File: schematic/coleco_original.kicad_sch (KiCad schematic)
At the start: 0 parts

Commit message: first day of pcb trace, working pin by of the z80 cpu. Last pin completed: 7
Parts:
- added J1: Cartridge Port, symbol Connector_Generic:Conn_02x15_Odd_Even
- added J2: Expansion Port, symbol Connector_Generic:Conn_02x30_Counter_Clockwise
- added JP1, JP2: SolderJumper_2_Open, symbol Jumper:SolderJumper_2_Open
- added R26: 470R, symbol Device:R
- added R60: 47R, symbol Device:R
- added U1: Z80CPU, symbol CPU:Z80CPU
- added U18, U19: 74LS541, symbol 74xx:74LS541
- added U2: 27C256, Package_DIP:DIP-28_W15.24mm, symbol Memory_EPROM:27C256
- added U20: SN76489AN, symbol Vintage_PC_Audio:SN76489AN
- added U3, U4: SCM2114AL, symbol Vintage_PC_RAM:SCM2114AL
- added U5: 74LS138, symbol 74xx:74LS138
- added U9: TMS9928A, symbol VINTAGE_PC_VIDEO:TMS9928A
- added WJ4, WJ5: Jumper_2_Bridged_32K_ROM, symbol Jumper:Jumper_2_Bridged
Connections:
- new net: U2.22 (~{OE}), U5.15 (O0), WJ4.2 (B)
- new net: J2.45 (Pin_45), R26.2, R60.2, U1.6 (~{CLK})
- new net: J2.40 (Pin_40), R26.1
- new net: JP1.1 (A), U2.20 (~{CE}), WJ4.1 (A)
- new net: JP2.2 (B), U2.23 (A11), WJ5.2 (B)
- new net +5VD: U2.1 (VPP), U2.26 (A13), U2.27 (A14), U2.28 (VCC)
- new net A0: U1.30 (A0)
- new net A1: U1.31 (A1)
- new net A10: U1.40 (A10)
- new net A11: J1.14 (Pin_14), J2.37 (Pin_37), JP1.2 (B), U1.1 (A11), WJ5.1 (A)
- new net A12: J1.24 (Pin_24), J2.38 (Pin_38), JP2.1 (A), U1.2 (A12), U2.2 (A12)
- new net A13: J1.19 (Pin_19), J2.22 (Pin_22), U1.3 (A13), U5.1 (A0)
- new net A14: J1.20 (Pin_20), J2.4 (Pin_4), U1.4 (A14), U5.2 (A1)
- new net A15: J2.43 (Pin_43), U1.5 (A15), U5.3 (A2)
- new net A2: U1.32 (A2)
- new net A3: U1.33 (A3)
- new net A4: U1.34 (A4)
- new net A5: U1.35 (A5)
- new net A6: U1.36 (A6)
- new net A7: U1.37 (A7)
- new net A8: U1.38 (A8)
- new net A9: U1.39 (A9)
- new net D0: U1.14 (D0), U2.11 (D0), U20.10 (D7), U9.17 (CD7)
- new net D1: U1.15 (D1), U2.12 (D1), U20.11 (D6), U9.18 (CD6)
- new net D2: U1.12 (D2), U2.13 (D2), U20.12 (D5), U9.19 (CD5)
- new net D3: U1.8 (D3), U2.15 (D3), U20.13 (D4), U9.20 (CD4)
- new net D4: J1.6 (Pin_6), J2.19 (Pin_19), U1.7 (D4), U18.15 (Y3), U19.14 (Y4), U2.16 (D4), U20.15 (D3), U4.14 (D0), U9.21 (CD3)
- new net D5: U1.9 (D5), U2.17 (D5), U20.1 (D2), U9.22 (CD2)
- new net D6: U1.10 (D6), U2.18 (D6), U20.2 (D1), U9.23 (CD1)
- new net D7: U1.13 (D7), U2.19 (D7), U20.3 (D0), U9.24 (CD0)

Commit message: revised schematic into sheets for easier design. Looks much better.
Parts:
- removed J1: Cartridge Port, symbol Connector_Generic:Conn_02x15_Odd_Even
- removed J2: Expansion Port, symbol Connector_Generic:Conn_02x30_Counter_Clockwise
- removed JP1, JP2: SolderJumper_2_Open, symbol Jumper:SolderJumper_2_Open
- removed R26: 470R, symbol Device:R
- removed R60: 47R, symbol Device:R
- removed U1: Z80CPU, symbol CPU:Z80CPU
- removed U18, U19: 74LS541, symbol 74xx:74LS541
- removed U2: 27C256, Package_DIP:DIP-28_W15.24mm, symbol Memory_EPROM:27C256
- removed U20: SN76489AN, symbol Vintage_PC_Audio:SN76489AN
- removed U3, U4: SCM2114AL, symbol Vintage_PC_RAM:SCM2114AL
- removed U5: 74LS138, symbol 74xx:74LS138
- removed U9: TMS9928A, symbol VINTAGE_PC_VIDEO:TMS9928A
- removed WJ4, WJ5: Jumper_2_Bridged_32K_ROM, symbol Jumper:Jumper_2_Bridged
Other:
- removed sheet io
- added sheet controller (controller.kicad_sch)
- added sheet decoder_logic (decoder_logic.kicad_sch)
- added sheet io_ports (io_ports.kicad_sch)
- sheet clock_reset ports: added ~{CLK}; removed none
- sheet cpu ports: added A[0..15], D[0..7], ~{CLK}; removed none
- sheet sound ports: added D[0..7]; removed audio, audio_data_bus, clk_audio, nWRITE_audio, ready
- sheet storage ports: added A[0..15], D[0..7], U5_O0; removed none
- sheet video ports: added D[0..7]; removed Y, Yb, Yr, mode, nCSR, nCSW, nINT, video_data_bus

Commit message: Up to pin 29 on z80 done. Address 0 to 10 left. Only tracing to its end point for the most part. Each chip gets traced chip to chip in this manned
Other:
- sheet clock_reset ports: added ~{INT}, ~{M1}, ~{RESET}, ~{RFSH}, ~{WAIT}; removed none
- sheet cpu ports: added ~{BUSAK}, ~{BUSRQ}, ~{HALT}, ~{INT}, ~{IORQ}, ~{M1}, ~{MREQ}, ~{NMI}, ~{RD}, ~{RESET}, ~{RFSH}, ~{WAIT}, ~{WR}; removed none
- sheet decoder_logic ports: added ~{IORQ}, ~{MREQ}, ~{WR}; removed none
- sheet io_ports ports: added WAIT, ~{BUSAK}, ~{BUSRQ}, ~{HALT}, ~{INT}, ~{IORQ}, ~{M1}, ~{MREQ}, ~{NMI}, ~{RD}, ~{RESET}, ~{RFSH}, ~{WR}; removed none
- sheet sound ports: added ~{WAIT}; removed none
- sheet storage ports: added ~{WR}; removed none
- sheet video ports: added ~{NMI}; removed none

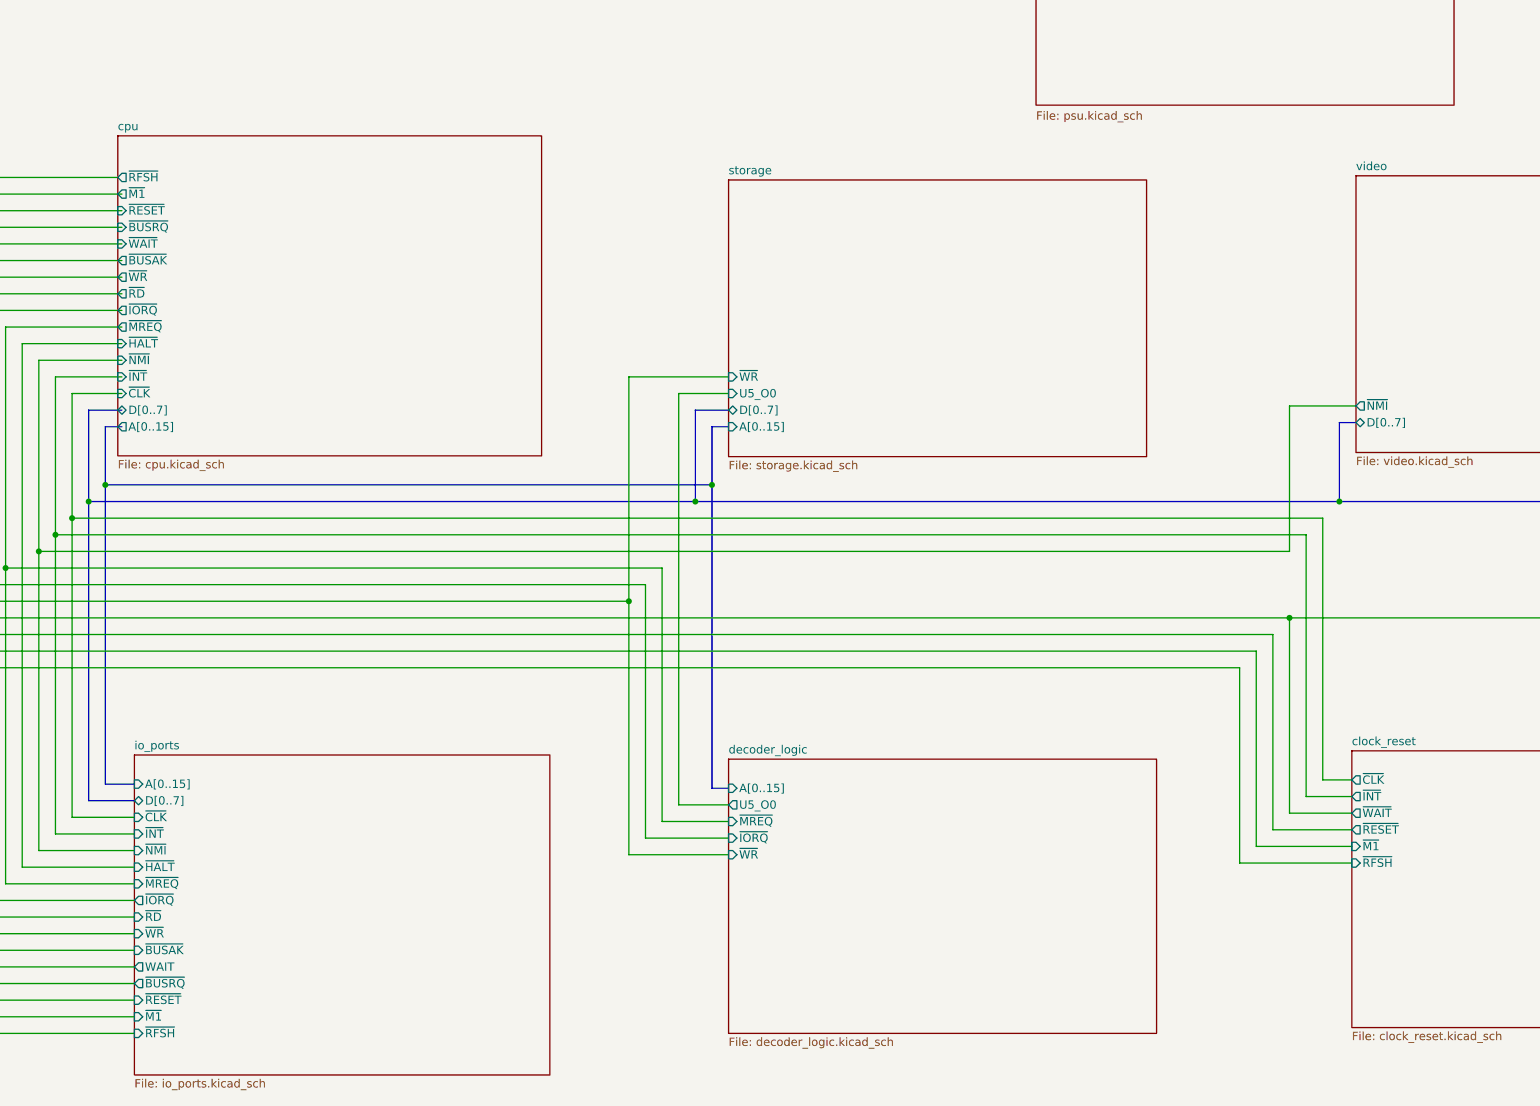
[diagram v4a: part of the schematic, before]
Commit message: completed Z80 trace of PCB. off to a good start.
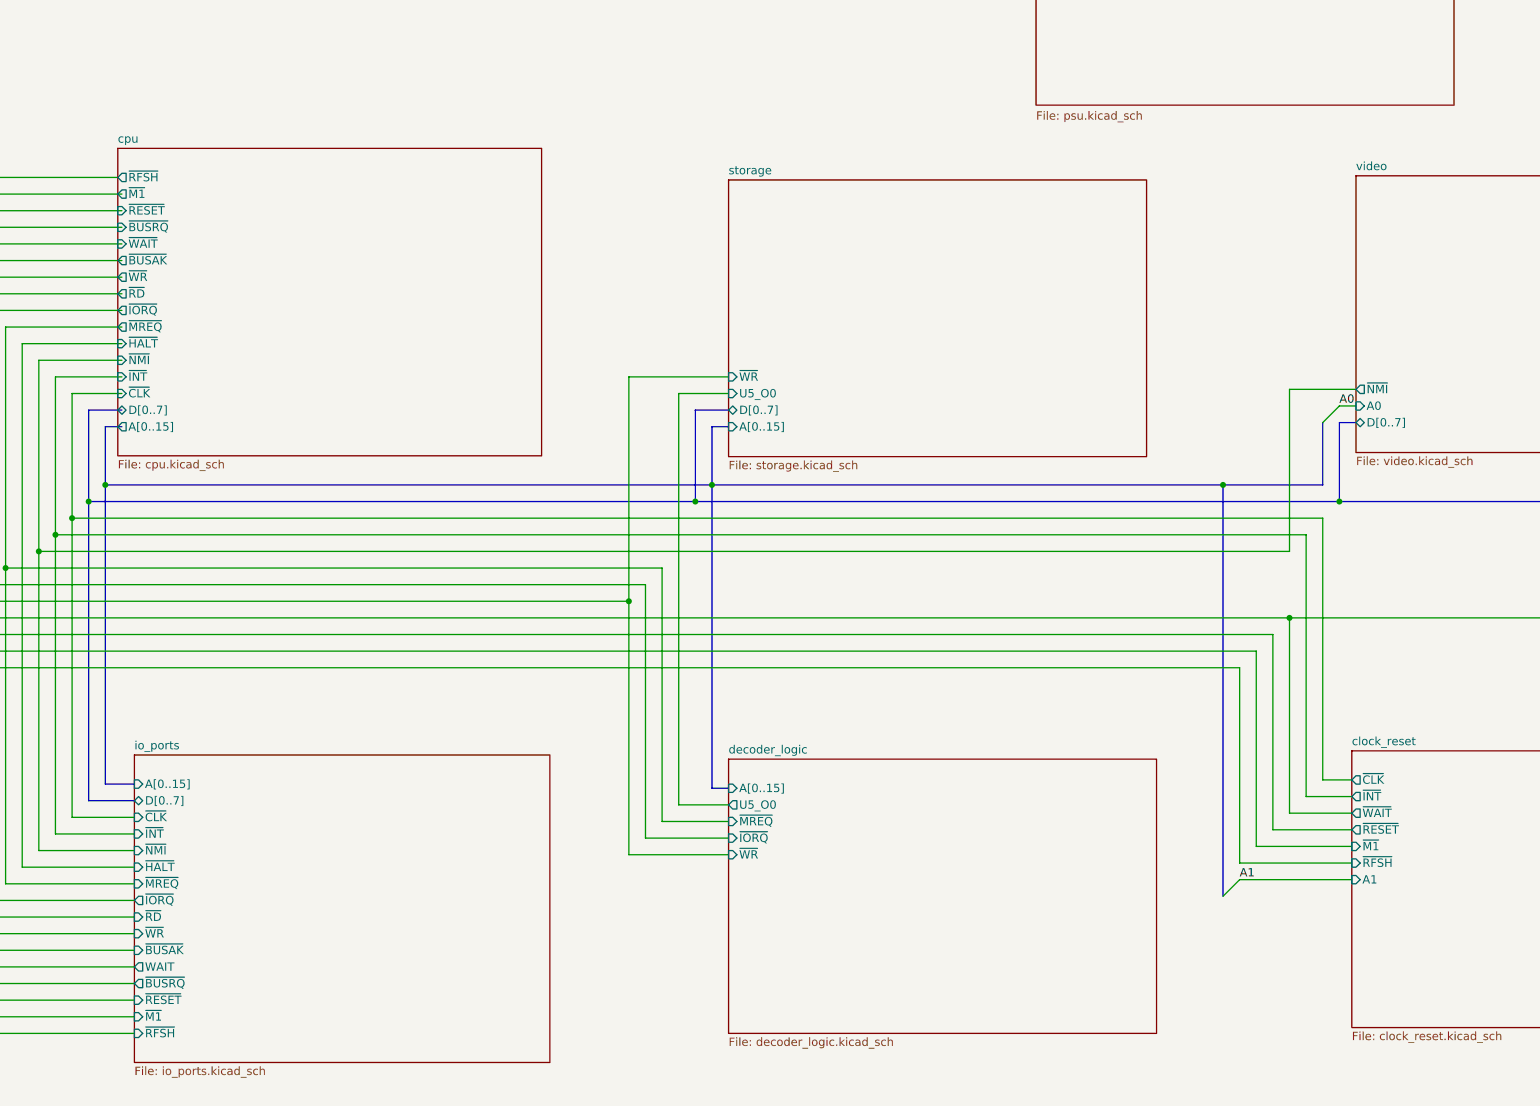
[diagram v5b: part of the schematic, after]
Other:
- sheet clock_reset ports: added A1; removed none
- sheet video ports: added A0; removed none
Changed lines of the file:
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@@
 (kicad_sch (version 20211123) (generator eeschema)
   (paper "B")
+  (junction (at 226.06 123.825) (diameter 0) (color 0 0 0 0)
+  )
   (junction (at 135.255 141.605) (diameter 0) (color 0 0 0 0)
   )
@@
   (junction (at 147.955 123.825) (diameter 0) (color 0 0 0 0)
   )
+  (bus_entry (at 226.06 186.69) (size 2.54 -2.54)
+    (stroke (width 0) (type default) (color 0 0 0 0))
+  )
+  (bus_entry (at 241.3 114.3) (size 2.54 -2.54)
+    (stroke (width 0) (type default) (color 0 0 0 0))
+  )
   (wire (pts (xy 24.765 84.455) (xy 57.785 84.455))
     (stroke (width 0) (type default) (color 0 0 0 0))
@@
     (stroke (width 0) (type default) (color 0 0 0 0))
   )
+  (bus (pts (xy 241.3 114.3) (xy 241.3 123.825))
+    (stroke (width 0) (type default) (color 0 0 0 0))
+  )
   (bus (pts (xy 145.415 112.395) (xy 145.415 126.365))
     (stroke (width 0) (type default) (color 0 0 0 0))
@@
     (stroke (width 0) (type default) (color 0 0 0 0))
   )
+  (bus (pts (xy 226.06 123.825) (xy 241.3 123.825))
+    (stroke (width 0) (type default) (color 0 0 0 0))
+  )
+  (bus (pts (xy 226.06 123.825) (xy 226.06 186.69))
+    (stroke (width 0) (type default) (color 0 0 0 0))
+  )
   (wire (pts (xy 17.145 151.765) (xy 228.6 151.765))
     (stroke (width 0) (type default) (color 0 0 0 0))
@@
     (stroke (width 0) (type default) (color 0 0 0 0))
   )
-  (wire (pts (xy 236.22 133.985) (xy 236.22 111.76))
+  (wire (pts (xy 236.22 133.985) (xy 236.22 109.22))
     (stroke (width 0) (type default) (color 0 0 0 0))
   )
@@
     (stroke (width 0) (type default) (color 0 0 0 0))
   )
+  (bus (pts (xy 147.955 123.825) (xy 226.06 123.825))
+    (stroke (width 0) (type default) (color 0 0 0 0))
+  )
   (bus (pts (xy 243.84 126.365) (xy 243.84 114.3))
     (stroke (width 0) (type default) (color 0 0 0 0))
@@
     (stroke (width 0) (type default) (color 0 0 0 0))
   )
+  (wire (pts (xy 228.6 184.15) (xy 245.745 184.15))
+    (stroke (width 0) (type default) (color 0 0 0 0))
+  )
   (wire (pts (xy 140.335 136.525) (xy 140.335 175.26))
     (stroke (width 0) (type default) (color 0 0 0 0))
@@
     (stroke (width 0) (type default) (color 0 0 0 0))
   )
+  (wire (pts (xy 243.84 111.76) (xy 246.38 111.76))
+    (stroke (width 0) (type default) (color 0 0 0 0))
+  )
   (wire (pts (xy 238.76 131.445) (xy 238.76 171.45))
     (stroke (width 0) (type default) (color 0 0 0 0))
@@
     (stroke (width 0) (type default) (color 0 0 0 0))
   )
-  (wire (pts (xy 236.22 111.76) (xy 246.38 111.76))
+  (wire (pts (xy 236.22 109.22) (xy 246.38 109.22))
     (stroke (width 0) (type default) (color 0 0 0 0))
   )
@@
     (stroke (width 0) (type default) (color 0 0 0 0))
   )
-  (sheet (at 57.15 70.485) (size 64.77 48.895) (fields_autoplaced)
+  (label "A0" (at 243.84 111.76 0)
+    (effects (font (size 1.27 1.27)) (justify left bottom))
+  )
+  (label "A1" (at 228.6 184.15 0)
+    (effects (font (size 1.27 1.27)) (justify left bottom))
+  )
+  (sheet (at 57.15 72.39) (size 64.77 46.99) (fields_autoplaced)
     (stroke (width 0) (type solid) (color 0 0 0 0))
     (fill (color 0 0 0 0.0000))
-    (property "Sheet name" "cpu" (id 0) (at 57.15 69.7734 0)
+    (property "Sheet name" "cpu" (id 0) (at 57.15 71.6784 0)
       (effects (font (size 1.27 1.27)) (justify left bottom))
     )
@@
       (effects (font (size 1.27 1.27)) (justify left))
     )
-    (pin "~{NMI}" output (at 246.38 111.76 180)
+    (pin "~{NMI}" output (at 246.38 109.22 180)
+      (effects (font (size 1.27 1.27)) (justify left))
+    )
+    (pin "A0" input (at 246.38 111.76 180)
       (effects (font (size 1.27 1.27)) (justify left))
     )
@@
       (effects (font (size 1.27 1.27)) (justify left))
     )
+    (pin "A1" input (at 245.745 184.15 180)
+      (effects (font (size 1.27 1.27)) (justify left))
+    )
   )
   (sheet (at 344.17 164.465) (size 64.77 41.91) (fields_autoplaced)
@@
     )
   )
-  (sheet (at 59.69 165.1) (size 63.5 48.895) (fields_autoplaced)
+  (sheet (at 59.69 165.1) (size 63.5 46.99) (fields_autoplaced)
     (stroke (width 0.1524) (type solid) (color 0 0 0 0))
     (fill (color 0 0 0 0.0000))
@@
       (effects (font (size 1.27 1.27)) (justify left bottom))
     )
-    (property "Sheet file" "io_ports.kicad_sch" (id 1) (at 59.69 214.5796 0)
-      (effects (font (size 1.27 1.27)) (justify left top))
-    )
+    (property "Sheet file" "io_ports.kicad_sch" (id 1) (at 59.69 212.6746 0)
+      (effects (font (size 1.27 1.27)) (justify left top))
+    )

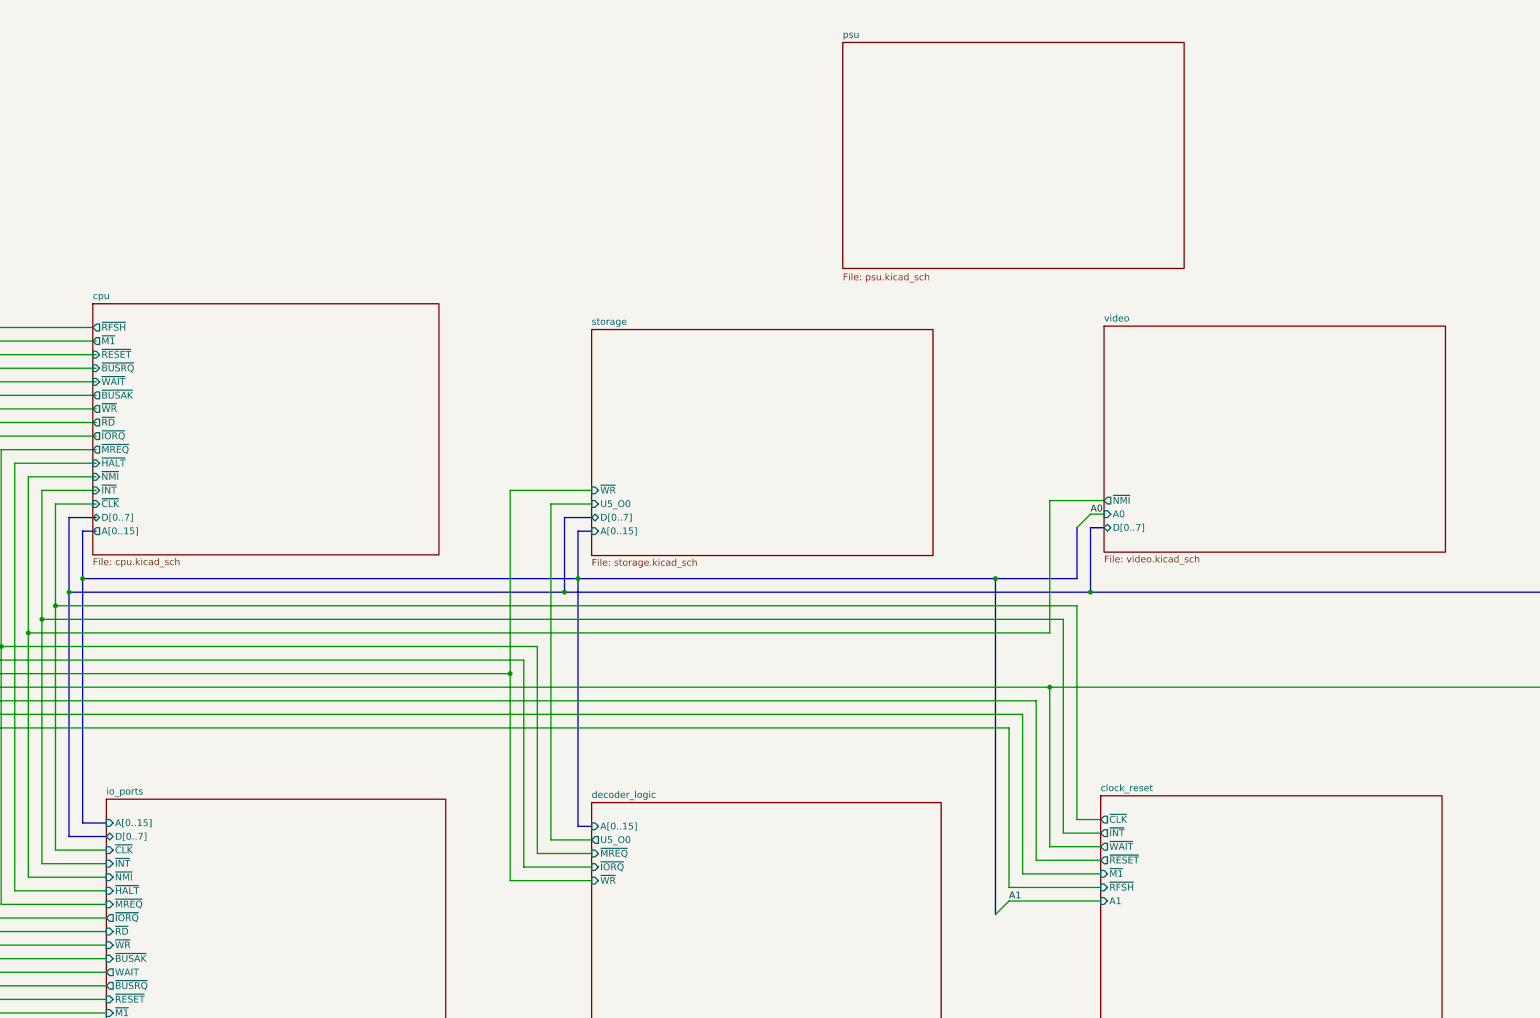
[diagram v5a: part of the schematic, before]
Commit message: added rf modulation schematic, added dram to vdp. Fixed +5vc to +5v
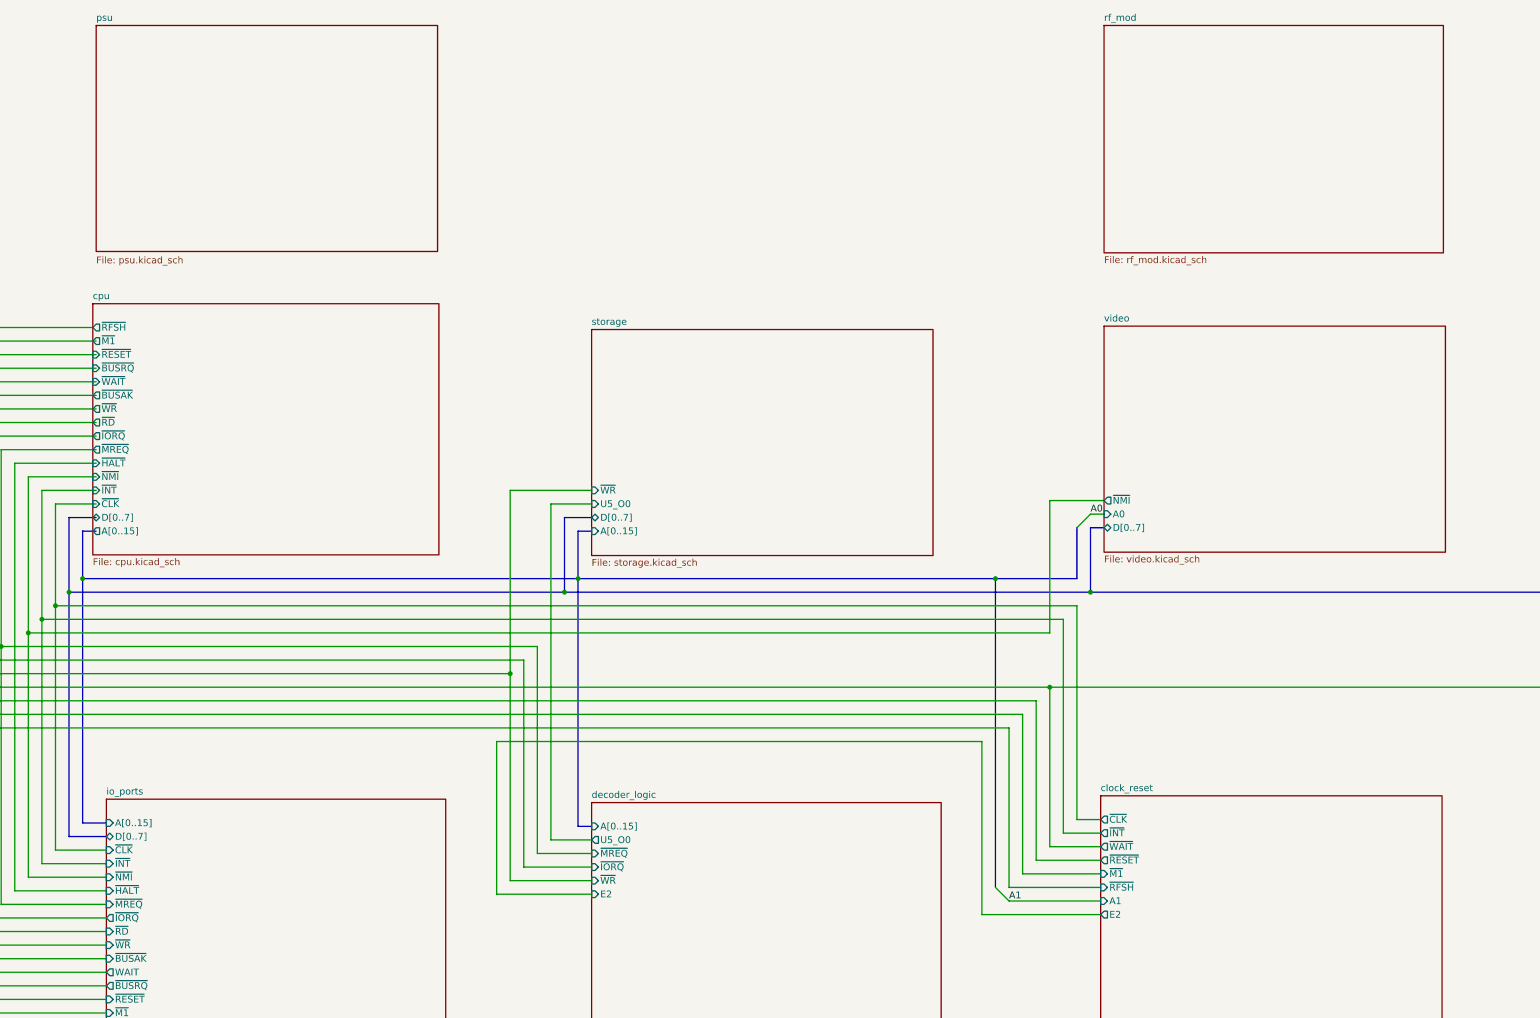
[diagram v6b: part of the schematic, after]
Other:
- added sheet rf_mod (rf_mod.kicad_sch)
- sheet clock_reset ports: added E2; removed none
- sheet decoder_logic ports: added E2; removed none
